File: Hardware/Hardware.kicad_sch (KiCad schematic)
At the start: 0 parts

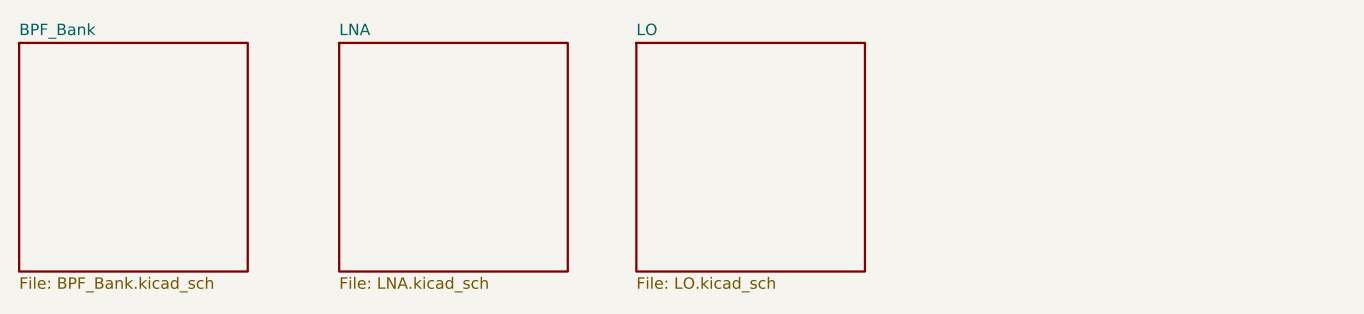
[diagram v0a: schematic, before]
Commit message: LO Loop Filter + Sims
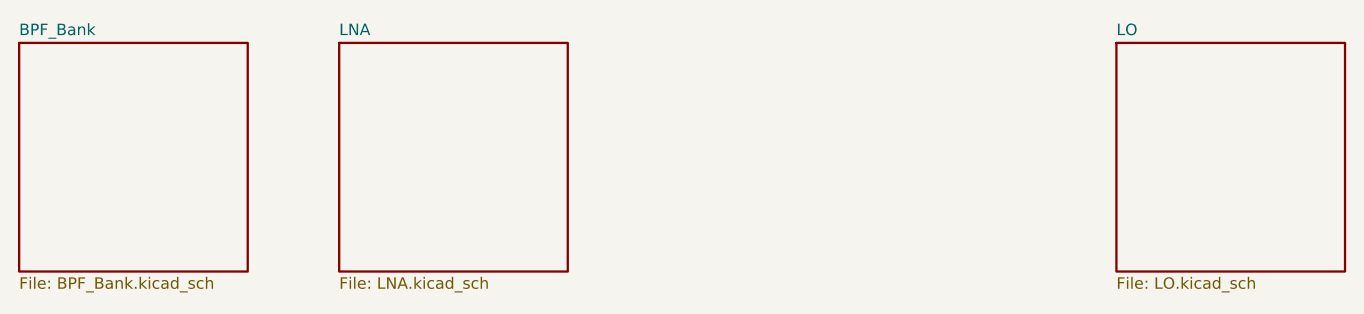
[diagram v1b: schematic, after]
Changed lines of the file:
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@@
 	)
 	(sheet
-		(at 93.98 25.4)
+		(at 147.32 25.4)
 		(size 25.4 25.4)
 		(exclude_from_sim no)
@@
 		)
 		(property "Sheetname" "LO"
-			(at 93.98 24.6884 0)
+			(at 147.32 24.6884 0)
 			(effects
 				(font
@@
 		)
 		(property "Sheetfile" "LO.kicad_sch"
-			(at 93.98 51.3846 0)
+			(at 147.32 51.3846 0)
 			(effects
 				(font
